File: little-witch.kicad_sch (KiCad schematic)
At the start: 24 parts, among them J1 USB_C_Receptacle_USB2.0_14P, J2 8P8C_LED, SW1 SW_Push, U1 CH32V307RCT6, Y1 SiT8008xx-1x-xxS

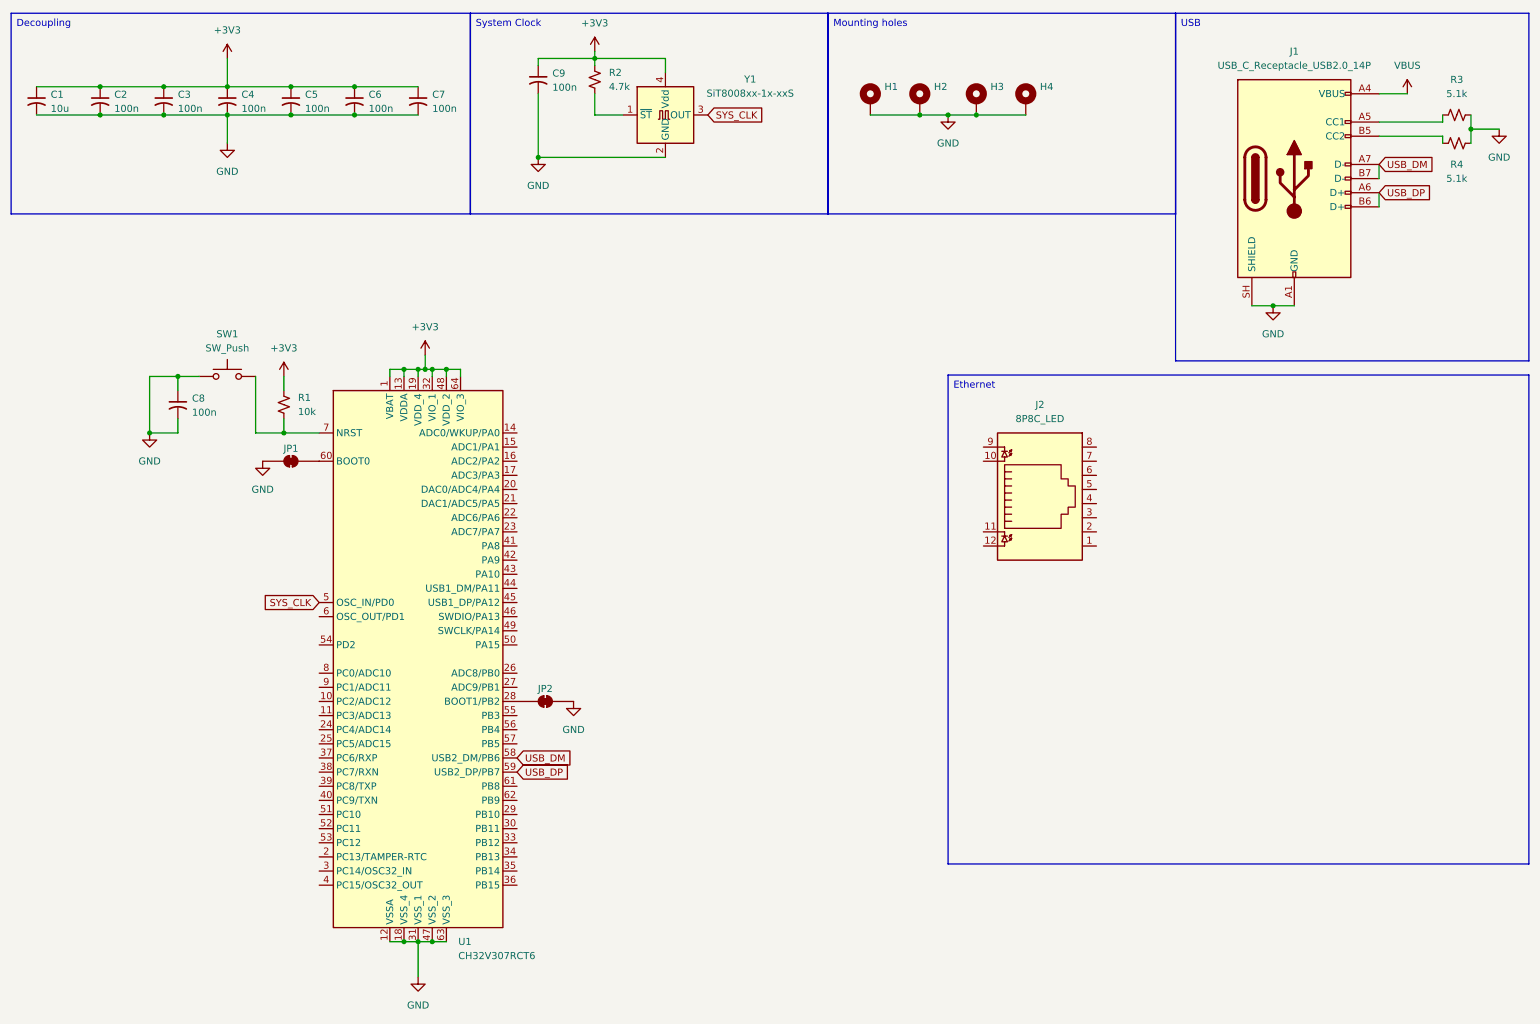
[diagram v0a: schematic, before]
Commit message: v0.1 without Ethernet or voltage reg
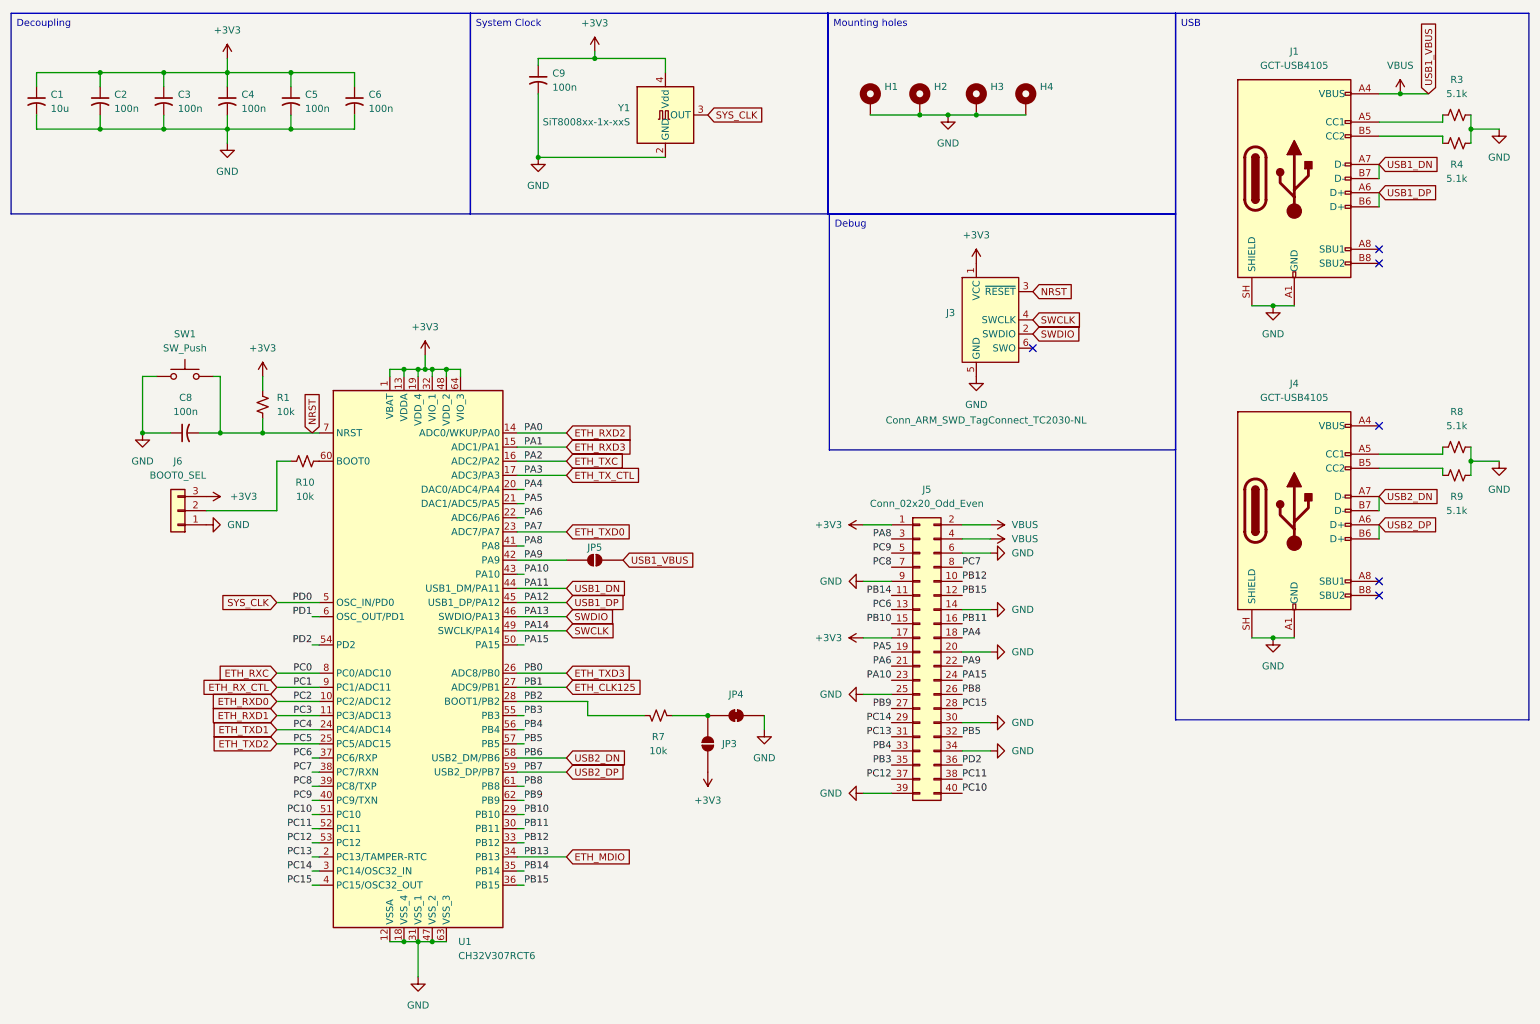
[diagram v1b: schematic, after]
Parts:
- removed C7: 100n, Capacitor_SMD:C_0402_1005Metric, symbol Device:C_Small_US
- removed J2: 8P8C_LED, snapmaker-footprints:TE_2041411-1, symbol Connector:RJ45_LED
- removed JP1, JP2: (no value), Jumper:SolderJumper-2_P1.3mm_Bridged_RoundedPad1.0x1.5mm, symbol Jumper:SolderJumper_2_Bridged
- removed R2: 4.7k, Resistor_SMD:R_0402_1005Metric, symbol Device:R_Small_US
- added J3: Conn_ARM_SWD_TagConnect_TC2030-NL, Connector:Tag-Connect_TC2030-IDC-NL_2x03_P1.27mm_Vertical, symbol Connector:Conn_ARM_SWD_TagConnect_TC2030-NL
- added J4: GCT-USB4105, Connector_USB:USB_C_Receptacle_GCT_USB4105-xx-A_16P_TopMnt_Horizontal, symbol Connector:USB_C_Receptacle_USB2.0_16P
- added J5: Conn_02x20_Odd_Even, Connector_PinHeader_2.54mm:PinHeader_2x20_P2.54mm_Vertical, symbol Connector_Generic:Conn_02x20_Odd_Even
- added J6: BOOT0_SEL, Connector_PinHeader_2.54mm:PinHeader_1x03_P2.54mm_Vertical, symbol Connector_Generic:Conn_01x03
- added JP3, JP5: SolderJumper_2_Open, Jumper:SolderJumper-2_P1.3mm_Open_RoundedPad1.0x1.5mm, symbol Jumper:SolderJumper_2_Open
- added JP4: SolderJumper_2_Open, Jumper:SolderJumper-2_P1.3mm_Bridged_RoundedPad1.0x1.5mm, symbol Jumper:SolderJumper_2_Bridged
- added R10, R7: 10k, Resistor_SMD:R_0402_1005Metric, symbol Device:R_Small_US
- added R8, R9: 5.1k, Resistor_SMD:R_0402_1005Metric, symbol Device:R_Small_US
- J1: value USB_C_Receptacle_USB2.0_14P -> GCT-USB4105; symbol Connector:USB_C_Receptacle_USB2.0_14P -> Connector:USB_C_Receptacle_USB2.0_16P
- Y1: symbol Oscillator:SiT8008xx-1x-xxS -> Oscillator:SiT8008xx-1x-xxN
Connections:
- net +3V3: now also J3.1 (VCC), J5.1 (Pin_1), J5.17 (Pin_17), J6.3 (Pin_3), JP3.1 (A)
- net GND: now also J3.5 (GND), J4.A1 (GND), J4.A12 (GND), J4.B1 (GND), J4.B12 (GND), J4.SH (SHIELD), J5.14 (Pin_14), J5.20 (Pin_20), J5.25 (Pin_25), J5.30 (Pin_30), J5.34 (Pin_34), J5.39 (Pin_39), J5.6 (Pin_6), J5.9 (Pin_9), J6.1 (Pin_1), JP4.1 (A), R8.2, R9.1; no longer C8.2
- net VBUS: now also J5.2 (Pin_2), J5.4 (Pin_4), JP5.1 (A)
- net ETH_RXD0: now reaches U1.10 (PC2/ADC12)
- net ETH_RXD1: now reaches U1.11 (PC3/ADC13)
- net ETH_RXD2: now reaches U1.14 (ADC0/WKUP/PA0)
- net ETH_RXD3: now reaches U1.15 (ADC1/PA1)
- net ETH_TXC: now reaches U1.16 (ADC2/PA2)
- net ETH_TX_CTL: now reaches U1.17 (ADC3/PA3)
- net PC13: now reaches U1.2 (PC13/TAMPER-RTC)
- net PC13: now also J5.31 (Pin_31)
- net PA4: now reaches U1.20 (DAC0/ADC4/PA4)
- net PA4: now also J5.18 (Pin_18)
- net PA5: now reaches U1.21 (DAC1/ADC5/PA5)
- net PA5: now also J5.19 (Pin_19)
- net PA6: now reaches U1.22 (ADC6/PA6)
- net PA6: now also J5.21 (Pin_21)
- net ETH_TXD0: now reaches U1.23 (ADC7/PA7)
- net ETH_TXD1: now reaches U1.24 (PC4/ADC14)
- net ETH_TXD2: now reaches U1.25 (PC5/ADC15)
- net ETH_TXD3: now reaches U1.26 (ADC8/PB0)
- net ETH_CLK125: now reaches U1.27 (ADC9/PB1)
- net PB2: now reaches U1.28 (BOOT1/PB2)
- net PB2: now also R7.2
- net PB10: now reaches U1.29 (PB10)
- net PB10: now also J5.15 (Pin_15)
- net PC14: now reaches U1.3 (PC14/OSC32_IN)
- net PC14: now also J5.29 (Pin_29)
- net PB11: now reaches U1.30 (PB11)
- net PB11: now also J5.16 (Pin_16)
- net PB12: now reaches U1.33 (PB12)
- net PB12: now also J5.10 (Pin_10)
- net ETH_MDIO: now reaches U1.34 (PB13)
- net PB14: now reaches U1.35 (PB14)
- net PB14: now also J5.11 (Pin_11)
- net PB15: now reaches U1.36 (PB15)
- net PB15: now also J5.12 (Pin_12)
- net PC6: now reaches U1.37 (PC6/RXP)
- net PC6: now also J5.13 (Pin_13)
- net PC7: now reaches U1.38 (PC7/RXN)
- net PC7: now also J5.8 (Pin_8)
- net PC8: now reaches U1.39 (PC8/TXP)
- net PC8: now also J5.7 (Pin_7)
- net PC15: now reaches U1.4 (PC15/OSC32_OUT)
- net PC15: now also J5.28 (Pin_28)
- net PC9: now reaches U1.40 (PC9/TXN)
- net PC9: now also J5.5 (Pin_5)
- net PA8: now reaches U1.41 (PA8)
- net PA8: now also J5.3 (Pin_3)
- net PA9: now reaches U1.42 (PA9)
- net PA9: now also J5.22 (Pin_22), JP5.2 (B)
- net PA10: now reaches U1.43 (PA10)
- net PA10: now also J5.23 (Pin_23)
- net USB1_DN: now reaches U1.44 (USB1_DM/PA11)
- net USB1_DN: now also J1.A7 (D-), J1.B7 (D-)
- net USB1_DP: now reaches U1.45 (USB1_DP/PA12)
- net USB1_DP: now also J1.A6 (D+), J1.B6 (D+)
- net SWDIO: now reaches U1.46 (SWDIO/PA13)
- net SWDIO: now also J3.2 (SWDIO)
- net SWCLK: now reaches U1.49 (SWCLK/PA14)
- net SWCLK: now also J3.4 (SWCLK)
- net PA15: now reaches U1.50 (PA15)
- net PA15: now also J5.24 (Pin_24)
- net PC10: now reaches U1.51 (PC10)
- net PC10: now also J5.40 (Pin_40)
- net PC11: now reaches U1.52 (PC11)
- net PC11: now also J5.38 (Pin_38)
- net PC12: now reaches U1.53 (PC12)
- net PC12: now also J5.37 (Pin_37)
- net PD2: now reaches U1.54 (PD2)
- net PD2: now also J5.36 (Pin_36)
- net PB3: now reaches U1.55 (PB3)
- net PB3: now also J5.35 (Pin_35)
- net PB4: now reaches U1.56 (PB4)
- net PB4: now also J5.33 (Pin_33)
- net PB5: now reaches U1.57 (PB5)
- net PB5: now also J5.32 (Pin_32)
- net PD1: now reaches U1.6 (OSC_OUT/PD1)
- net at U1.60 (BOOT0): now also R10.2
- net PB8: now reaches U1.61 (PB8)
- net PB8: now also J5.26 (Pin_26)
- net PB9: now reaches U1.62 (PB9)
- net PB9: now also J5.27 (Pin_27)
- net NRST: now reaches R1.2, SW1.2, U1.7 (NRST)
- net NRST: now also C8.2, J3.3 (~{RESET})
- net ETH_RXC: now reaches U1.8 (PC0/ADC10)
- net ETH_RX_CTL: now reaches U1.9 (PC1/ADC11)
- removed net USB_DM: J1.A7 (D-), J1.B7 (D-), U1.58 (USB2_DM/PB6)
- removed net USB_DP: J1.A6 (D+), J1.B6 (D+), U1.59 (USB2_DP/PB7)
- new net: J4.B5 (CC2), R9.2
- new net: JP3.2 (B), JP4.2 (B), R7.1
- new net: J6.2 (Pin_2), R10.1
- new net: J4.A5 (CC1), R8.1
- new net: J4.A4 (VBUS), J4.A9 (VBUS), J4.B4 (VBUS), J4.B9 (VBUS)
- new net USB2_DN: J4.A7 (D-), J4.B7 (D-), U1.58 (USB2_DM/PB6)
- new net USB2_DP: J4.A6 (D+), J4.B6 (D+), U1.59 (USB2_DP/PB7)
- no-connect marks 0 -> 6
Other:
- moved on the sheet: R1, SW1

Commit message: Import all symbols into project library
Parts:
- U1: symbol wch_mcu:CH32V307RCT6 -> Library:CH32V307RCT6
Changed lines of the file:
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@@
 	)
 	(symbol
-		(lib_id "wch_mcu:CH32V307RCT6")
+		(lib_id "Library:CH32V307RCT6")
 		(at 85.09 127 0)
 		(unit 1)

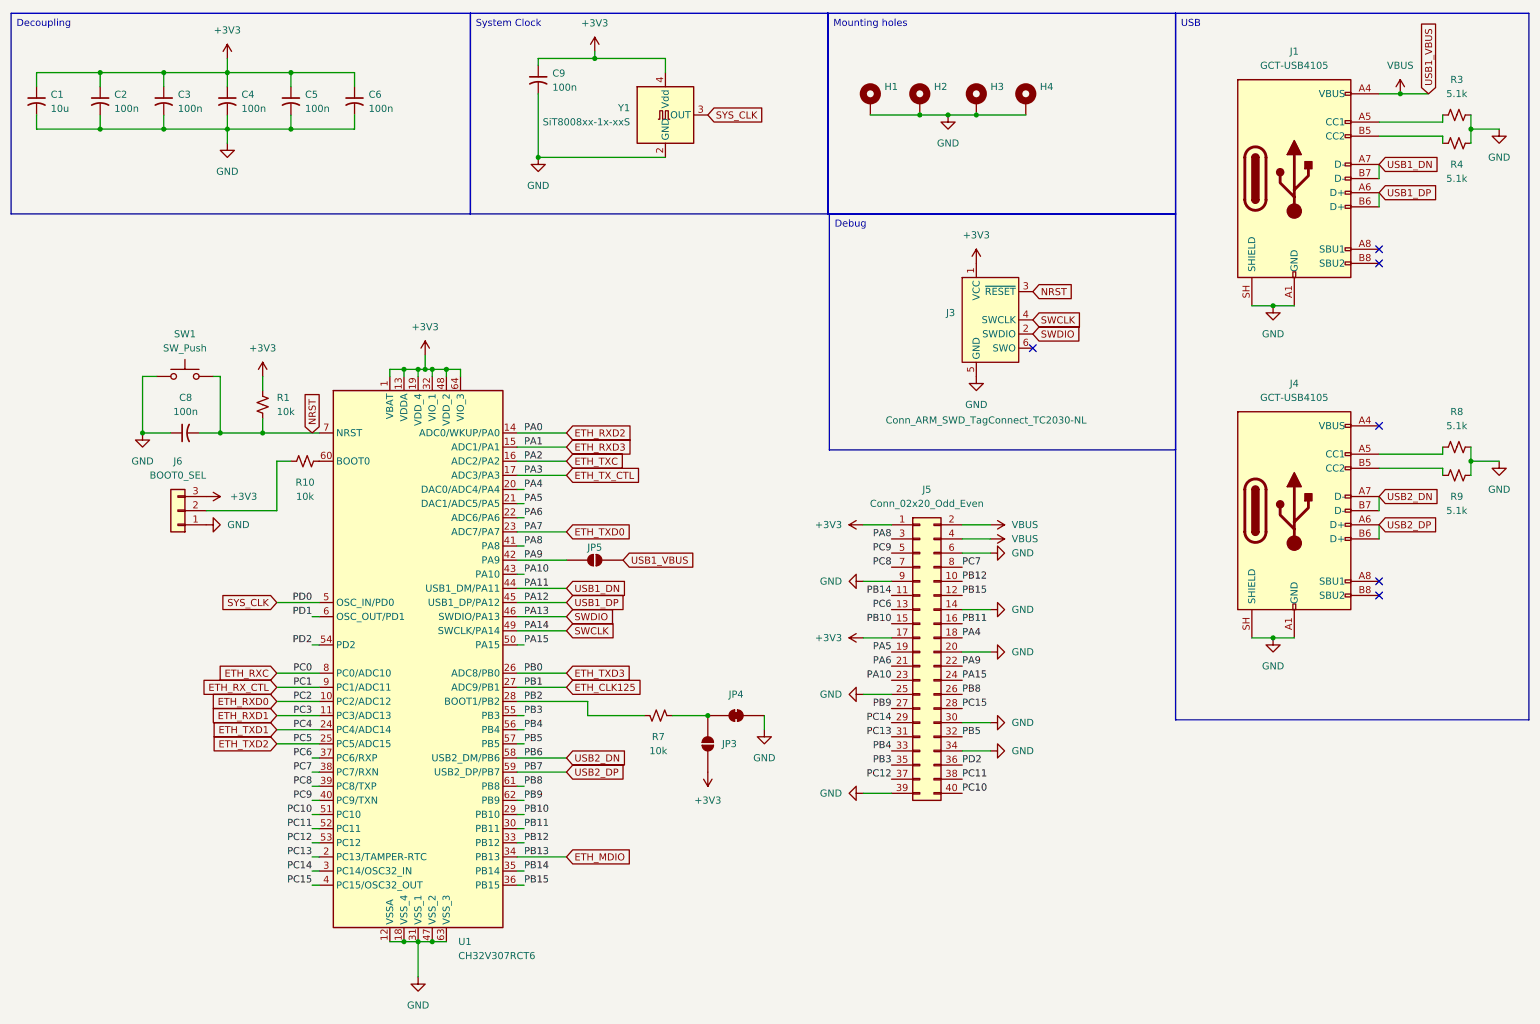
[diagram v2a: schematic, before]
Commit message: Ethernet schematic done
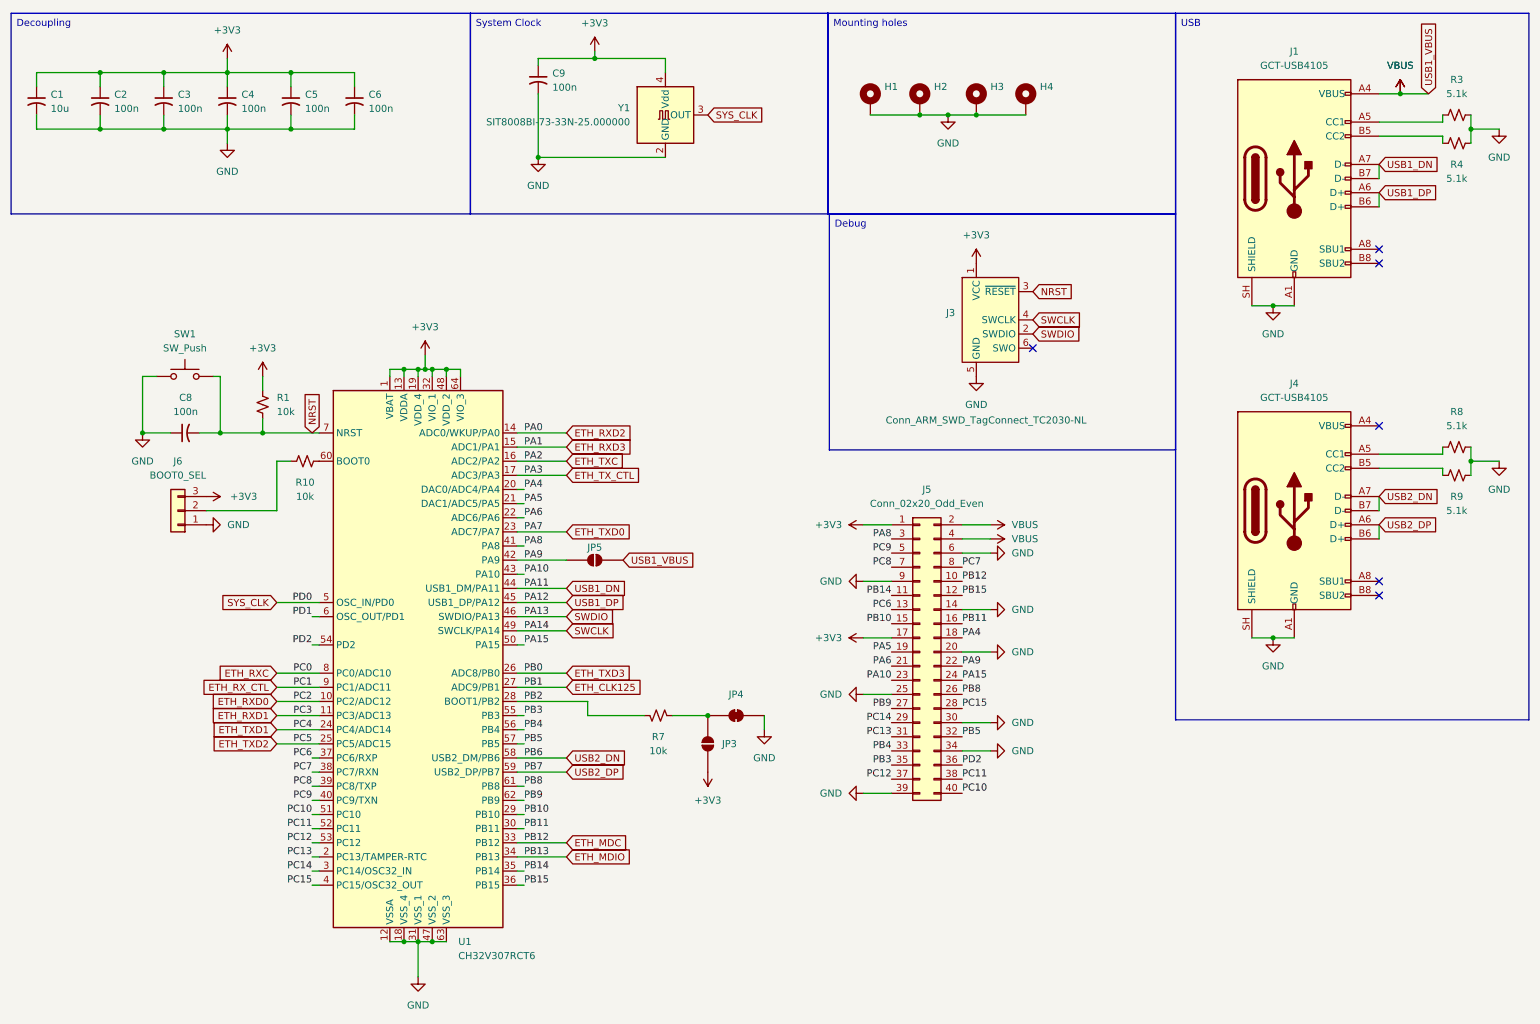
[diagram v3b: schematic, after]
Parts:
- Y1: value SiT8008xx-1x-xxS -> SIT8008BI-73-33N-25.000000; footprint Oscillator:Oscillator_SMD_SiT_PQFN-4Pin_2.5x2.0mm -> Oscillator:Oscillator_SMD_SiT_PQFN-4Pin_2.0x1.6mm
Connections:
- net PB12 renamed ETH_MDC
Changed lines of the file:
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@@
 	(wire
 		(pts
-			(xy 104.14 161.29) (xy 102.87 161.29)
+			(xy 102.87 161.29) (xy 111.76 161.29)
 		)
 		(stroke
@@
 		)
 	)
+	(global_label "ETH_MDC"
+		(shape input)
+		(at 111.76 161.29 0)
+		(fields_autoplaced yes)
+		(effects
+			(font
+				(size 1.27 1.27)
+			)
+			(justify left)
+		)
+		(property "Intersheetrefs" "${INTERSHEET_REFS}"
+			(at 123.1513 161.29 0)
+			(hide yes)
+			(show_name no)
+			(do_not_autoplace no)
+			(effects
+				(font
+					(size 1.27 1.27)
+				)
+				(justify left)
+			)
+		)
+	)
 	(global_label "SWDIO"
 		(shape input)
@@
 			)
 		)
-		(property "Value" "SiT8008xx-1x-xxS"
+		(property "Value" "SIT8008BI-73-33N-25.000000"
 			(at 123.19 31.7499 0)
 			(show_name no)
@@
 			)
 		)
-		(property "Footprint" "Oscillator:Oscillator_SMD_SiT_PQFN-4Pin_2.5x2.0mm"
+		(property "Footprint" "Oscillator:Oscillator_SMD_SiT_PQFN-4Pin_2.0x1.6mm"
 			(at 129.54 30.48 0)
 			(hide yes)
@@
 			)
 		)
-		(property "Description" "SiTime Low Power Mems programmable oscillator, 1MHz to 110MHz, PQFN-4, 2.5x2.0mm (with NC pin)"
+		(property "Description" "SiTime Low Power Mems programmable oscillator, 2.5MHz, PQFN-4, 2.0x1.6mm (with NC pin)"
 			(at 129.54 30.48 0)
 			(hide yes)
@@
 					(unit 1)
 				)
+			)
+		)
+	)
+	(symbol
+		(lib_id "power:VBUS")
+		(at 261.62 26.67 0)
+		(unit 1)
+		(body_style 1)
+		(exclude_from_sim no)
+		(in_bom yes)
+		(on_board yes)
+		(in_pos_files yes)
+		(dnp no)
+		(fields_autoplaced yes)
+		(property "Reference" "#PWR011"
+			(at 261.62 30.48 0)
+			(hide yes)
+			(show_name no)
+			(do_not_autoplace no)
+			(effects
+				(font
+					(size 1.27 1.27)
+				)
+			)
+		)
+		(property "Value" "VBUS"
+			(at 261.62 21.59 0)
+			(show_name no)
+			(do_not_autoplace no)
+			(effects
+				(font
+					(size 1.27 1.27)
+				)
+			)
+		)
+		(property "Footprint" ""
+			(at 261.62 26.67 0)
+			(hide yes)
+			(show_name no)
+			(do_not_autoplace no)
+			(effects
+				(font
+					(size 1.27 1.27)
+				)
+			)
+		)
+		(property "Datasheet" ""
+			(at 261.62 26.67 0)
+			(hide yes)
+			(show_name no)
+			(do_not_autoplace no)
+			(effects
+				(font
+					(size 1.27 1.27)
+				)
+			)
+		)
+		(property "Description" "Power symbol creates a global label with name \"VBUS\""
+			(at 261.62 26.67 0)
+			(hide yes)
+			(show_name no)
+			(do_not_autoplace no)
+			(effects
+				(font
+					(size 1.27 1.27)
+				)
+			)
+		)
+		(pin "1"
+		)
+		(instances
+			(project "little-witch"
+				(path "/eaea4e42-a070-4be5-b9dd-9215ef3d72c7"
+					(reference "#PWR011")
+					(unit 1)
+				)
